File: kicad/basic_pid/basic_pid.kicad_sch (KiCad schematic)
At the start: 41 parts, among them J1 Input A, J2 Input B / Setpoint, J3 Error monitor, J4 Output, SW1 SW_DPDT_x2, SW2 SW_DPDT_x2, SW3 SW_SPDT, SW4 SW_SP3T, U1 LM4040LP-5, U10 OPA189, U11 BUF634A, U2 LM4040LP-5, U3 LT1167, U4 LT1167, U5 OPA189, U6 OPA189, U7 OPA189, U8 OPA189, U9 OPA189

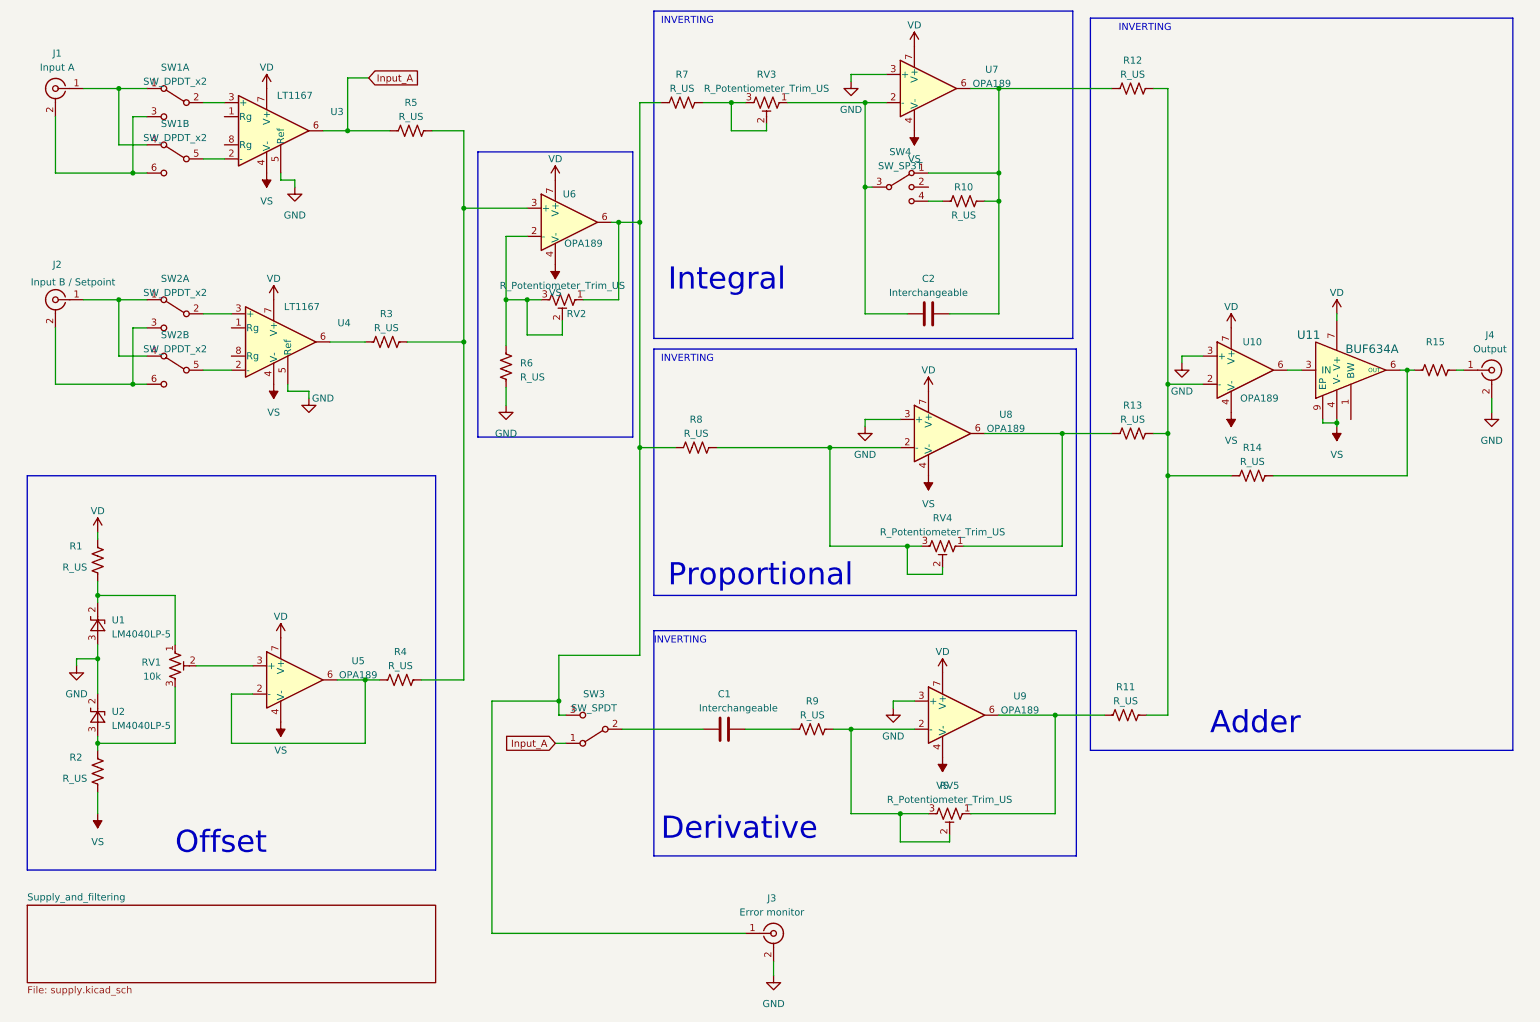
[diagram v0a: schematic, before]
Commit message: Schematic almost finalized:
Ended up using switches to select pre-set capacitors rather than ZIFs

TO DO:
1) design the power supply and filtering section.
2) Layout work (consider adding capacitors for stabilization...)
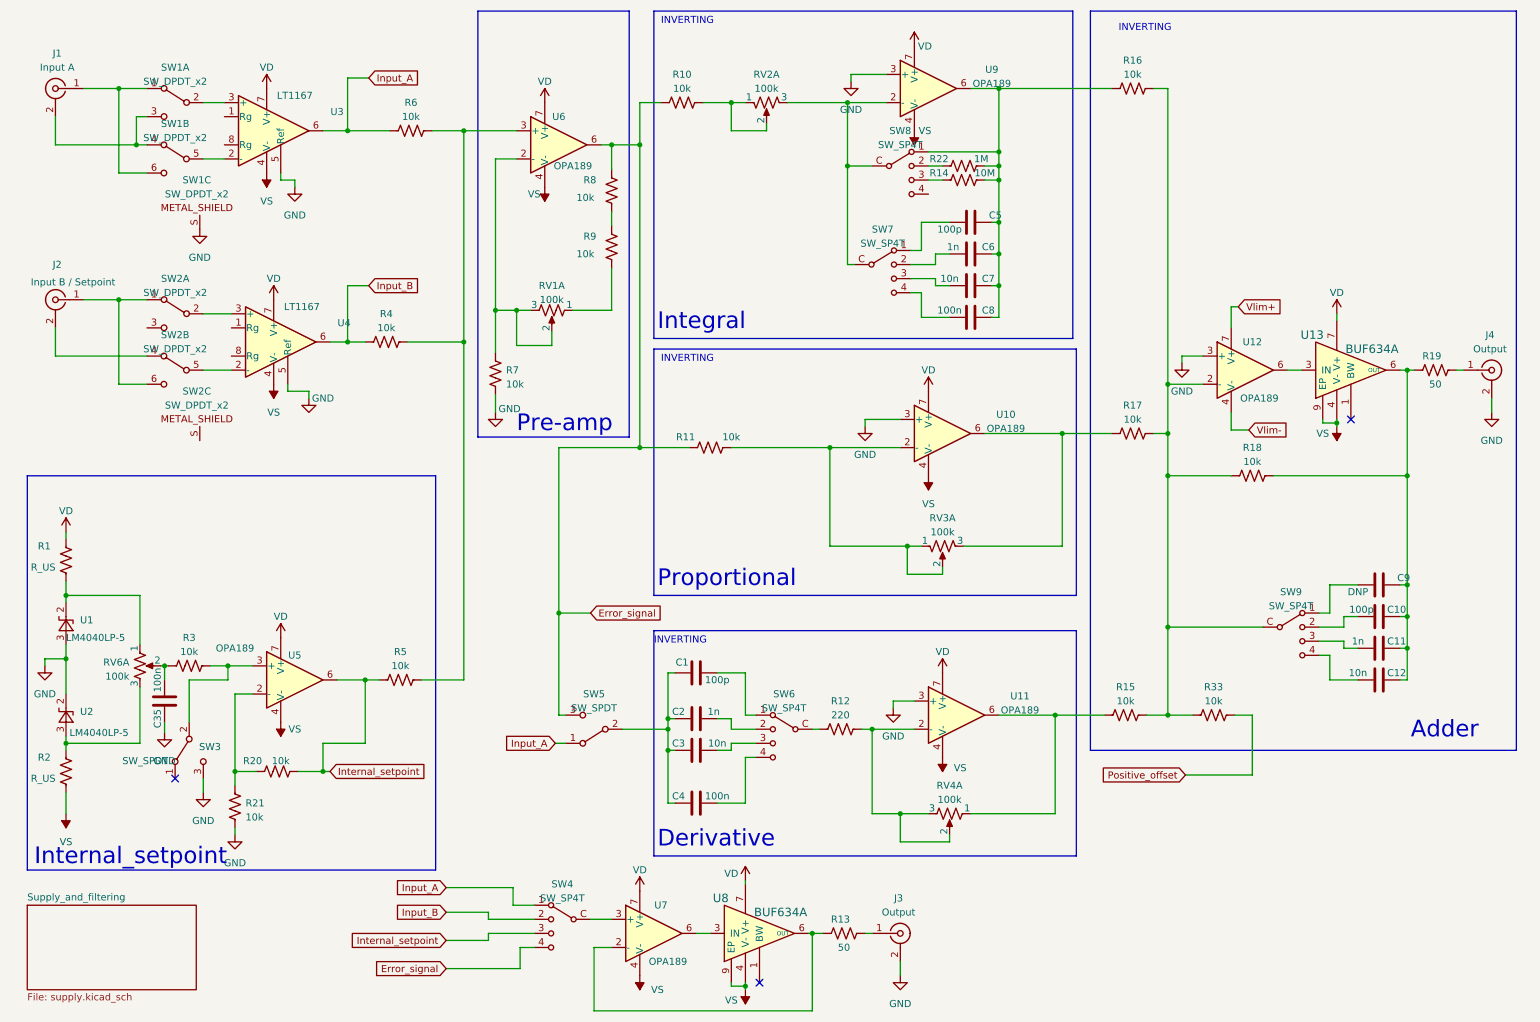
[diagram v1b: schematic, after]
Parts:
- removed RV1: 10k, symbol Device:R_Potentiometer_Trim_US
- removed RV2, RV3, RV4, RV5: R_Potentiometer_Trim_US, symbol Device:R_Potentiometer_Trim_US
- removed SW1, SW2: SW_DPDT_x2, symbol Switch:SW_DPDT_x2
- removed SW4: SW_SP3T, symbol Switch:SW_SP3T
- removed U11: BUF634A, lib:BUF634U, symbol buf634A:BUF634A
- added C10, C5: 100p, Capacitor_SMD:C_0805_2012Metric, symbol Device:C
- added C11, C6: 1n, Capacitor_SMD:C_0805_2012Metric, symbol Device:C
- added C12, C3, C7: 10n, Capacitor_SMD:C_0805_2012Metric, symbol Device:C
- added C35, C4, C8: 100n, Capacitor_SMD:C_0805_2012Metric, symbol Device:C
- added C9: DNP, Capacitor_SMD:C_0805_2012Metric, symbol Device:C
- added R11, R20, R21, R3, R33, R9: 10k, Resistor_SMD:R_0805_2012Metric, symbol Device:R_US
- added R13: 50, Resistor_SMD:R_0805_2012Metric, symbol Device:R_US
- added R22: 1M, Resistor_SMD:R_0805_2012Metric, symbol Device:R_US
- added RV1, RV2, RV3, RV4, RV6: 100k, lib:Slide_pot_45mm, symbol local_lib:potentiometer_and _LED
- added SW1, SW2: SW_DPDT_x2, lib:MHS222, symbol local_lib:SW_DPDT_x2
- added SW3: SW_SPDT, symbol Switch:SW_SPDT
- added SW4, SW6, SW7, SW8, SW9: SW_SP4T, lib:SLB1470, symbol local_lib:SW_SP4T
- added U13, U8: BUF634A, lib:TI_SO-PowerPAD-8_ThermalVias, symbol local_lib:BUF634A
- added U7: OPA189, Package_SO:SOIC-8_3.9x4.9mm_P1.27mm, symbol Amplifier_Operational:OPA330xxD
- C1: value Interchangeable -> 100p; footprint Connector_Wire:SolderWire-2.5sqmm_1x02_P7.2mm_D2.4mm_OD3.6mm -> Capacitor_SMD:C_0805_2012Metric
- C2: value Interchangeable -> 1n; footprint Connector_Wire:SolderWire-2.5sqmm_1x02_P7.2mm_D2.4mm_OD3.6mm -> Capacitor_SMD:C_0805_2012Metric
- J3: value Error monitor -> Output
- R1, R2: footprint (none) -> Resistor_SMD:R_0805_2012Metric
- R10: renamed from R7; value R_US -> 10k; footprint (none) -> Resistor_SMD:R_0805_2012Metric
- R12: renamed from R9; value R_US -> 220; footprint (none) -> Resistor_SMD:R_0805_2012Metric
- R14: renamed from R10; value R_US -> 10M; footprint (none) -> Resistor_SMD:R_0805_2012Metric
- R15: renamed from R11; value R_US -> 10k; footprint (none) -> Resistor_SMD:R_0805_2012Metric
- R16: renamed from R12; value R_US -> 10k; footprint (none) -> Resistor_SMD:R_0805_2012Metric
- R17: renamed from R13; value R_US -> 10k; footprint (none) -> Resistor_SMD:R_0805_2012Metric
- R18: renamed from R14; value R_US -> 10k; footprint (none) -> Resistor_SMD:R_0805_2012Metric
- R19: renamed from R15; footprint (none) -> Resistor_SMD:R_0805_2012Metric
- R4: renamed from R3; value R_US -> 10k; footprint (none) -> Resistor_SMD:R_0805_2012Metric
- R5: renamed from R4; value R_US -> 10k; footprint (none) -> Resistor_SMD:R_0805_2012Metric
- R6: renamed from R5; value R_US -> 10k; footprint (none) -> Resistor_SMD:R_0805_2012Metric
- R7: renamed from R6; value R_US -> 10k; footprint (none) -> Resistor_SMD:R_0805_2012Metric
- R8: value R_US -> 10k; footprint (none) -> Resistor_SMD:R_0805_2012Metric
- renumbered SW3 to SW5, U8 to U10, U9 to U11, U10 to U12, U7 to U9
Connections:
- net GND: now also C35.1, R21.1, SW1.S, SW3.3 (C)
- net Input_A: now also SW4.1
- net VD: now also U13.7 (V+), U7.7 (V+), U8.7 (V+); no longer U12.7 (V+)
- net VS: now also U13.4 (V-), U13.9 (EP), U7.4 (V-), U8.4 (V-), U8.9 (EP); no longer U12.4 (V-)
- net Internal_setpoint: now reaches R5.1, U5.6
- net Internal_setpoint: now also R20.2, SW4.3; no longer U5.2 (-)
- net at U5.3 (+): now also R3.2, SW3.2 (B)
- net at R15.2, R16.2, R17.2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: now also R33.1, SW9.C (Common)
- net at R18.2, R19.1: now also C10.1, C11.1, C12.1, C9.1, U13.6 (OUT)
- net at R12.1: now also SW6.C (Common); no longer C1.2
- net at R12.2, U11.2 (-): now also RV4.2, RV4.3
- net at R15.1, U11.6: now also RV4.1
- net at J1.1 (In): now also SW1.1 (A), SW1.6 (C)
- net at J1.2 (Ext): now also SW1.3 (C), SW1.4 (A)
- net Error_signal: now reaches R10.1, SW5.3 (C), U6.6
- net Error_signal: now also R8.2, R11.1, SW4.4; no longer J3.1 (In), R8.1
- net at R7.2, U6.2 (-): now also RV1.2, RV1.3
- net at R2.2, U2.3 (A): now also RV6.3
- net at R14.2, R16.1, U9.6: now also C5.1, C6.1, C7.1, C8.1, R22.2, SW8.1; no longer C2.2
- net at C2.1: now also C1.1, SW5.2 (B), C3.1, C4.1; no longer U9.2 (-)
- net at R14.1: now also SW8.3
- net at J2.1 (In): now also SW2.1 (A), SW2.6 (C)
- net at U4.3 (+): now also SW2.2 (B)
- net at J2.2 (Ext): now also SW2.4 (A)
- net at U3.3 (+): now also SW1.2 (B)
- net at R17.1, U10.6: now also RV3.3
- net at U10.2 (-): now also R11.2, RV3.1, RV3.2; no longer R8.2
- net at U4.2 (-): now also SW2.5 (B)
- net Input_B: now reaches R4.1, U4.6
- net Input_B: now also SW4.2
- net at U12.6: now also U13.3 (IN)
- net at R10.2: now also RV2.1, RV2.2
- net at R1.1, U1.2 (K): now also RV6.1
- net at U3.2 (-): now also SW1.5 (B)
- new net: C35.2, R3.1, RV6.2
- new net: R20.1, R21.2, U5.2 (-)
- new net: R9.1, RV1.1
- new net: C10.2, SW9.2
- new net: R8.1, R9.2
- new net: C12.2, SW9.4
- new net: R13.1, U7.2 (-), U8.6 (OUT)
- new net: J3.1 (In), R13.2
- new net: SW4.C (Common), U7.3 (+)
- new net: U7.6, U8.3 (IN)
- new net: C9.2, SW9.1
- new net: C11.2, SW9.3
- new net: C4.2, SW6.4
- new net: RV2.3, SW7.C (Common), SW8.C (Common), U9.2 (-)
- new net: C8.2, SW7.4
- new net: C3.2, SW6.3
- new net: C1.2, SW6.1
- new net: C2.2, SW6.2
- new net: C6.2, SW7.2
- new net: R22.1, SW8.2
- new net: C5.2, SW7.1
- new net: C7.2, SW7.3
- new net Positive_offset: R33.2
- new net Vlim+: U12.7 (V+)
- new net Vlim-: U12.4 (V-)
- no-connect marks 0 -> 3
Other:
- note added: "Internal_setpoint"
- note added: "Pre-amp"
- note removed: "Offset"
- moved on the sheet: R1, R12, R14, R2, R7, U1, U2, U6

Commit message: Schematic finalized and layout work begun
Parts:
- removed unit 3 of SW1
- removed unit 3 of SW2
- removed SW3, SW5: SW_SPDT, symbol Switch:SW_SPDT
- added R33, R34: DNP, Resistor_SMD:R_0805_2012Metric, symbol Device:R_US
- added SW3, SW5: SW_DPDT_x2, lib:MHS222, symbol local_lib:SW_DPDT_x2
- C2: renamed from C1; value 100p -> DNP
- C3: renamed from C2; value 1n -> 100p
- C4: renamed from C3; value 10n -> 1n
- C5: renamed from C4; value 100n -> 10n
- C6: renamed from C5; value 100p -> 1nF
- C7: renamed from C6; value 1n -> 10nF
- C8: renamed from C7; value 10n -> 100nF
- C9: renamed from C8; value 100n -> 1uF
- J1, J2, J3, J4: footprint lib:BNC_Amphenol_B6252HB-NPP3G-50_Horizontal -> lib:BNC_Amphenol_031-5539_Vertical
- R10: renamed from R8; DIGIKEY (none) -> 2019-RN73H2ATTD1002B25CT-ND
- R11: renamed from R9; DIGIKEY (none) -> 2019-RN73H2ATTD1002B25CT-ND
- R12: renamed from R10; DIGIKEY (none) -> 2019-RN73H2ATTD1002B25CT-ND
- R13: renamed from R11; DIGIKEY (none) -> 2019-RN73H2ATTD1002B25CT-ND
- R16: renamed from R22; DIGIKEY (none) -> YAG3766CT-ND; PARTNO (none) -> AC0805JR-071ML
- R17: renamed from R14; DIGIKEY (none) -> 311-10MARCT-ND; PARTNO (none) -> RC0805JR-0710ML
- R18: renamed from R15; DIGIKEY (none) -> 2019-RN73H2ATTD1002B25CT-ND
- R19: renamed from R16; DIGIKEY (none) -> 2019-RN73H2ATTD1002B25CT-ND
- R20: renamed from R17; DIGIKEY (none) -> 2019-RN73H2ATTD1002B25CT-ND
- R21: renamed from R33; DIGIKEY (none) -> 2019-RN73H2ATTD1002B25CT-ND
- R22: renamed from R18; DIGIKEY (none) -> 2019-RN73H2ATTD1002B25CT-ND
- R3: DIGIKEY (none) -> 2019-RN73H2ATTD1002B25CT-ND
- R4: renamed from R21; DIGIKEY (none) -> 2019-RN73H2ATTD1002B25CT-ND
- R5: renamed from R20; DIGIKEY (none) -> 2019-RN73H2ATTD1002B25CT-ND
- R6: renamed from R4; DIGIKEY (none) -> 2019-RN73H2ATTD1002B25CT-ND
- R7: renamed from R5; DIGIKEY (none) -> 2019-RN73H2ATTD1002B25CT-ND
- R8: renamed from R6; DIGIKEY (none) -> 2019-RN73H2ATTD1002B25CT-ND
- R9: renamed from R7; DIGIKEY (none) -> 2019-RN73H2ATTD1002B25CT-ND
- renumbered C35 to C1, C9 to C10, C10 to C11, C11 to C12, C12 to C13, R12 to R14, R13 to R15, R19 to R23, RV6 to RV1, RV1 to RV2, RV2 to RV3, RV3 to RV4, RV4 to RV5
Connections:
- net Error_signal: now also SW3.1 (A)
- net GND: now also SW5.3 (C)
- net Input_A: now also SW3.3 (C)
- net at SW2.3 (C): now also J2.2 (Ext), SW2.4 (A)
- net at R3.2, U5.3 (+): now also SW5.2 (B)
- net at U4.1 (Rg): now also R34.2
- net at U4.8 (Rg): now also R34.1
- net at C2.1, C3.1, C4.1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: now also SW3.2 (B)
- net at U3.1 (Rg): now also R33.2
- net at U3.8 (Rg): now also R33.1
- net VD renamed +12V
- net VS renamed -12V
- no-connect marks 3 -> 4
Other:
- moved on the sheet: C10, C11, C12, C13, R4, SW9
